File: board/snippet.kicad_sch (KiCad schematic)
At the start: 9 parts, among them Q1 TPN3300ANH,LQ, Q2 TPN3300ANH,LQ, Q3 TPN3300ANH,LQ, Q4 TPN3300ANH,LQ, Q5 TPN3300ANH,LQ, Q6 TPN3300ANH,LQ, Q7 TPN3300ANH,LQ, Q8 TPN3300ANH,LQ, U1 LT4321

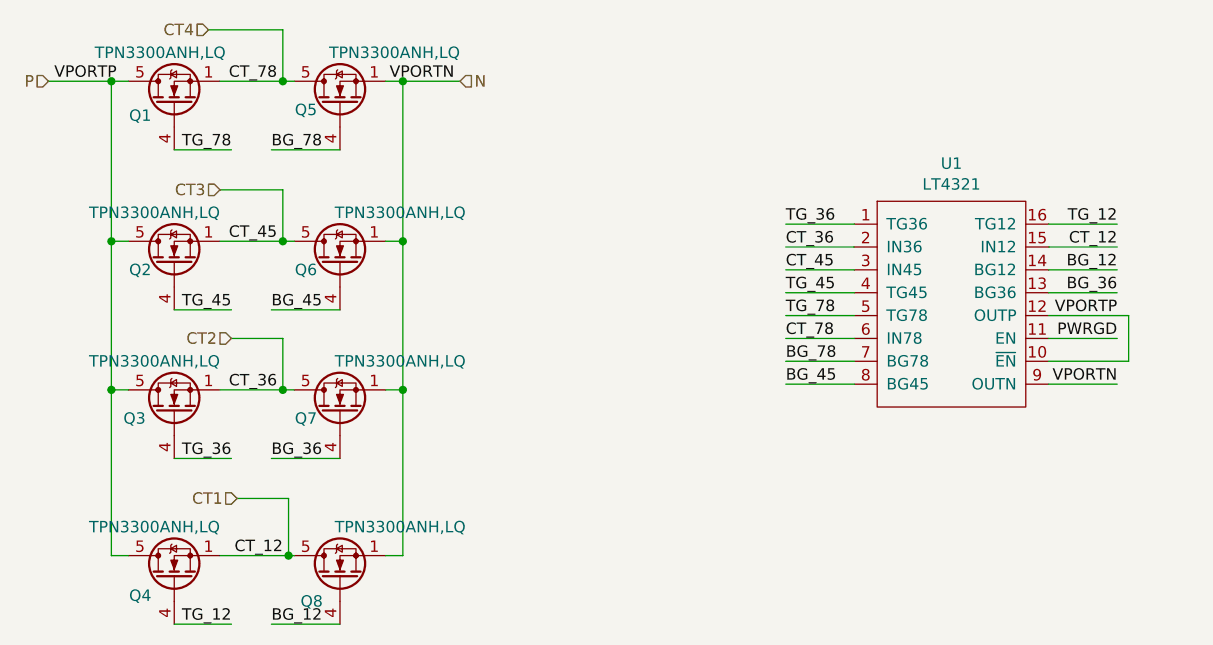
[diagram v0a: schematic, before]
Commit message: updated connectors, changed mosfets and added enable resistors
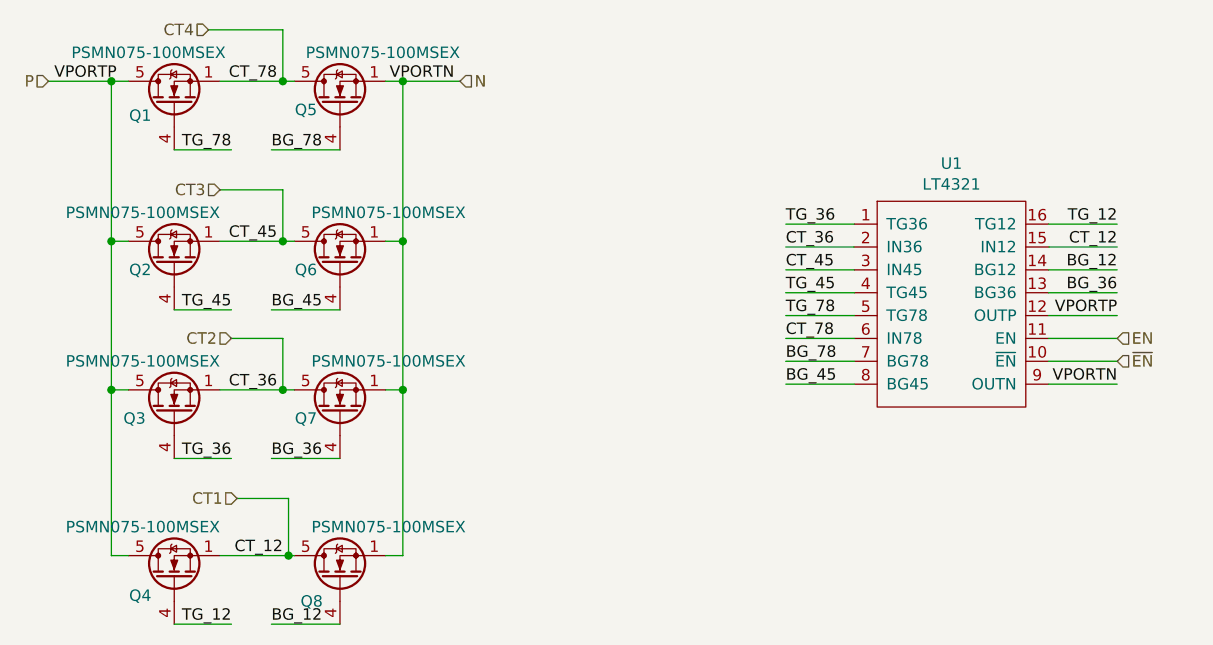
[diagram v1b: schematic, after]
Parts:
- Q1, Q2, Q3, Q4, Q5, Q6, Q7, Q8: value TPN3300ANH,LQ -> PSMN075-100MSEX; MPN TPN3300ANH,LQ -> PSMN075-100MSEX
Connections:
- net P: no longer U1.10 (~{EN})
- net PWRGD renamed EN
- new net ~{EN}: U1.10 (~{EN})
